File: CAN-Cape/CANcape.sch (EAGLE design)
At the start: 3 parts

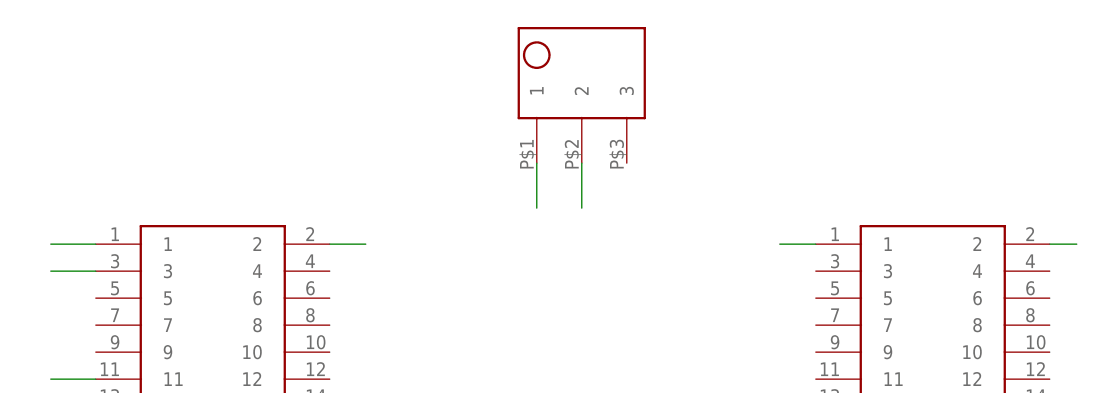
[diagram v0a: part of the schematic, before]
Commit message: added OBDII connector
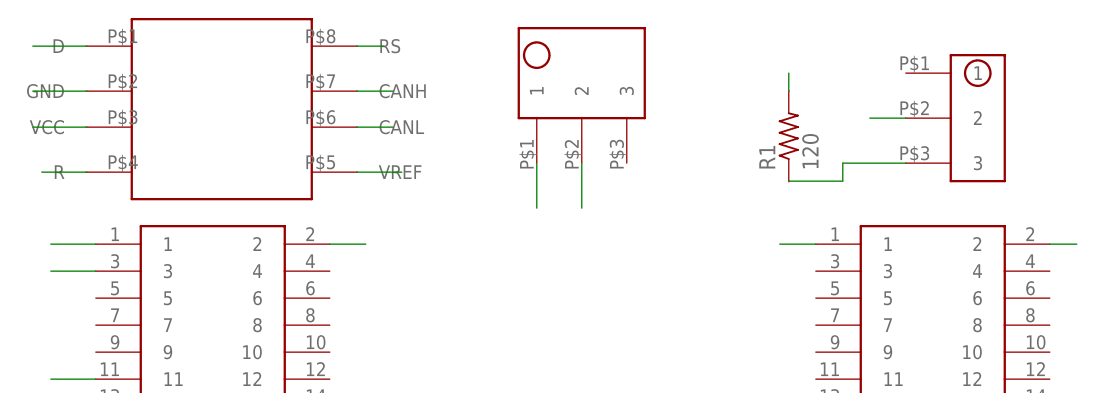
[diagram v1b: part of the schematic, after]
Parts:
- added R1: 120, resistor:R-US_0207/12
- added U$4: 1X3_HEADER, CANcape:1X3_HEADER
- added U$5: SN65HVD320, SPST-switch:SN65HVD320
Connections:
- new net N$1: U$4.3
- net CANH: now also U$4.2
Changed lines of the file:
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@@
 <layer number="97" name="Info" color="7" fill="1" visible="no" active="yes"/>
 <layer number="98" name="Guide" color="6" fill="1" visible="no" active="yes"/>
+<layer number="99" name="SpiceOrder" color="5" fill="1" visible="yes" active="yes"/>
 </layers>
 <schematic xreflabel="%F%N/%S.%C%R" xrefpart="/%S.%C%R">
@@
 <part name="U$2" library="CANcape" deviceset="2X23_STACKABLE_HEADERS" device=""/>
 <part name="U$3" library="CANcape" deviceset="TB-5.0-PT-3P" device=""/>
+<part name="U$4" library="CANcape" deviceset="1X3_HEADER" device=""/>
+<part name="R1" library="resistor" deviceset="R-US_" device="0207/12" value="120"/>
+<part name="U$5" library="SPST-switch" deviceset="SN65HVD320" device=""/>
 </parts>
 <sheets>
@@
 <instance part="U$2" gate="G$1" x="107" y="66"/>
 <instance part="U$3" gate="G$1" x="67" y="105" rot="R90"/>
+<instance part="U$4" gate="G$1" x="112" y="100"/>
+<instance part="R1" gate="G$1" x="91" y="98" rot="R90"/>
+<instance part="U$5" gate="G$1" x="28" y="101"/>
 </instances>
 <busses>
@@
 <wire x1="40" y1="53" x2="45" y2="53" width="0.1524" layer="91"/>
 </segment>
+<segment>
+<wire x1="13" y1="94" x2="8" y2="94" width="0.1524" layer="91"/>
+</segment>
 </net>
 <net name="DCAN1_TX" class="0">
@@
 <pinref part="U$1" gate="G$1" pin="26"/>
 <wire x1="40" y1="50" x2="45" y2="50" width="0.1524" layer="91"/>
+</segment>
+<segment>
+<wire x1="13" y1="108" x2="7" y2="108" width="0.1524" layer="91"/>
 </segment>
 </net>
@@
 <wire x1="63" y1="95" x2="63" y2="90" width="0.1524" layer="91"/>
 </segment>
+<segment>
+<pinref part="U$4" gate="G$1" pin="2"/>
+<wire x1="104" y1="100" x2="100" y2="100" width="0.1524" layer="91"/>
+</segment>
+<segment>
+<wire x1="43" y1="103" x2="47" y2="103" width="0.1524" layer="91"/>
+</segment>
 </net>
 <net name="CANL" class="0">
@@
 <pinref part="U$3" gate="G$1" pin="2"/>
 <wire x1="68" y1="95" x2="68" y2="90" width="0.1524" layer="91"/>
+</segment>
+<segment>
+<wire x1="91" y1="103" x2="91" y2="105" width="0.1524" layer="91"/>
+</segment>
+<segment>
+<wire x1="43" y1="99" x2="47" y2="99" width="0.1524" layer="91"/>
 </segment>
 </net>
@@
 <wire x1="40" y1="86" x2="44" y2="86" width="0.1524" layer="91"/>
 </segment>
+<segment>
+<wire x1="13" y1="103" x2="7" y2="103" width="0.1524" layer="91"/>
+</segment>
 </net>
 <net name="3.3V" class="0">
@@
 <pinref part="U$1" gate="G$1" pin="3"/>
 <wire x1="14" y1="83" x2="9" y2="83" width="0.1524" layer="91"/>
+</segment>
+<segment>
+<wire x1="13" y1="99" x2="7" y2="99" width="0.1524" layer="91"/>
+</segment>
+<segment>
+<wire x1="43" y1="94" x2="48" y2="94" width="0.1524" layer="91"/>
 </segment>
 </net>
@@
 <wire x1="14" y1="71" x2="9" y2="71" width="0.1524" layer="91"/>
 </segment>
+<segment>
+<wire x1="43" y1="108" x2="46" y2="108" width="0.1524" layer="91"/>
+</segment>
 </net>
+<net name="N$1" class="0">
+<segment>
+<wire x1="91" y1="93" x2="97" y2="93" width="0.1524" layer="91"/>
+<wire x1="97" y1="93" x2="97" y2="95" width="0.1524" layer="91"/>
+<pinref part="U$4" gate="G$1" pin="3"/>
+<wire x1="97" y1="95" x2="104" y2="95" width="0.1524" layer="91"/>
+</segment>
+</net>
